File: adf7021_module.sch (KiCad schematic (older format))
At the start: 59 parts, among them J1 Conn_02x10_Counter_Clockwise, J2 Conn_Coaxial, J3 Conn_Coaxial, J4 Conn_02x10_Counter_Clockwise, U1 ADF7021, X1 19.68MHz

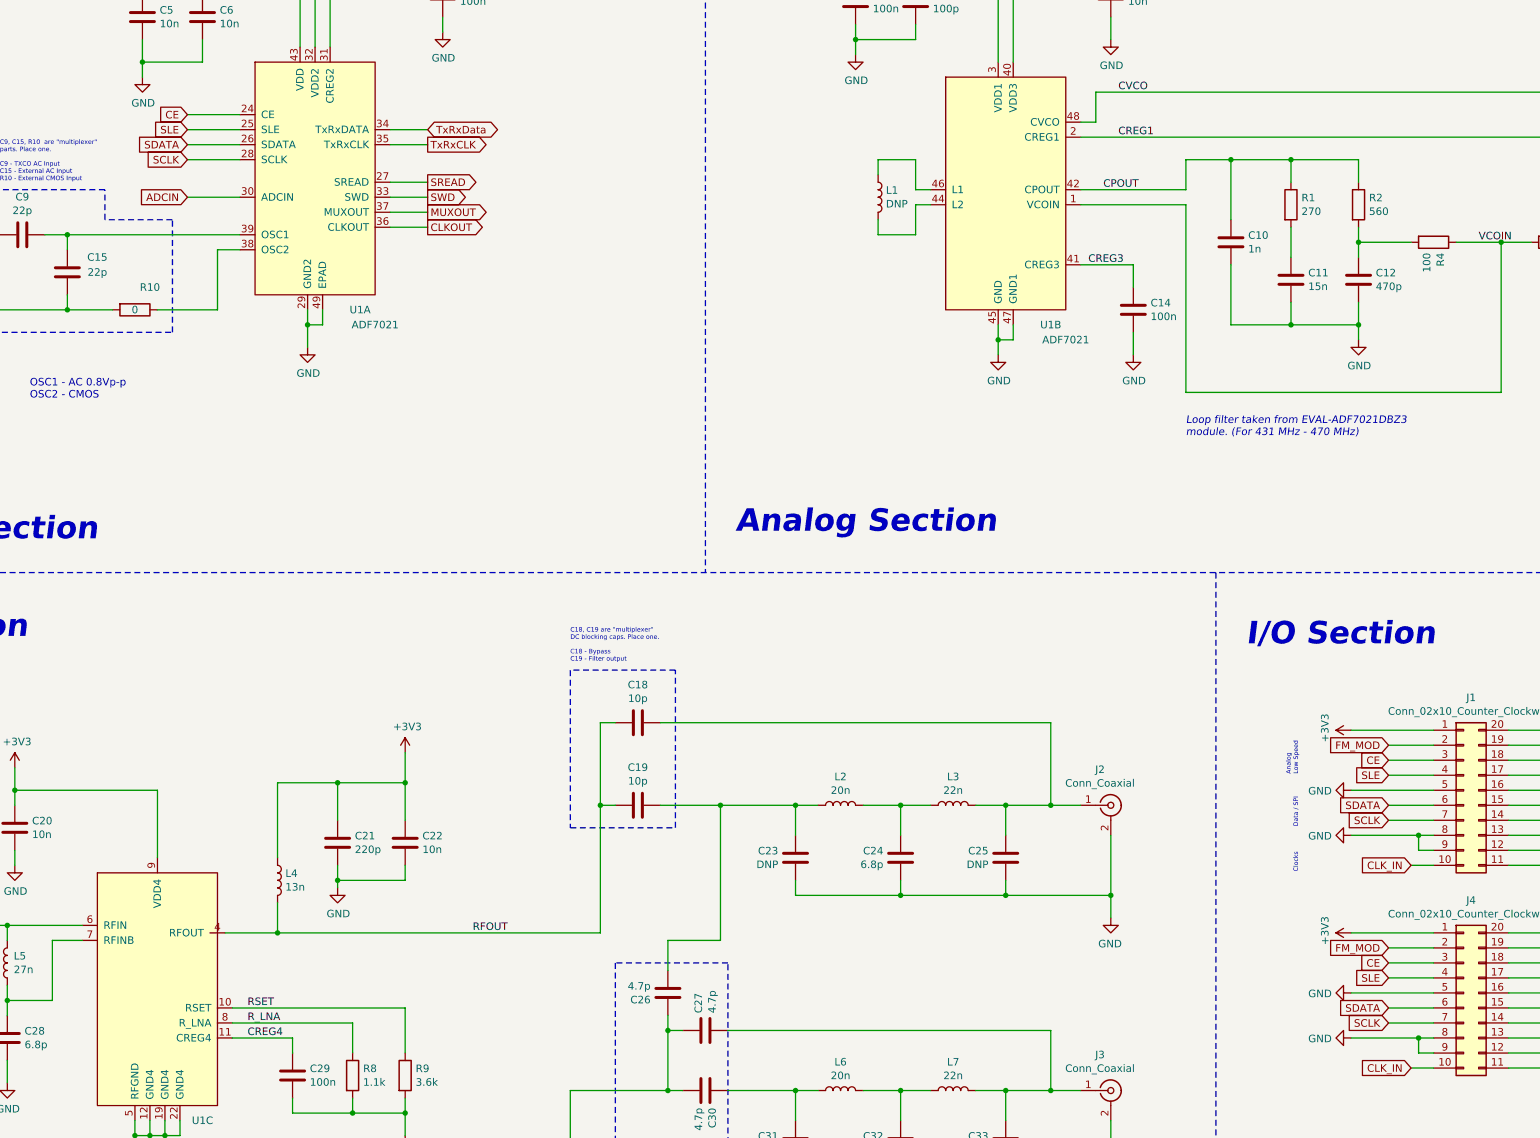
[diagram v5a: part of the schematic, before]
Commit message: Adding series resistors on clock / data pins
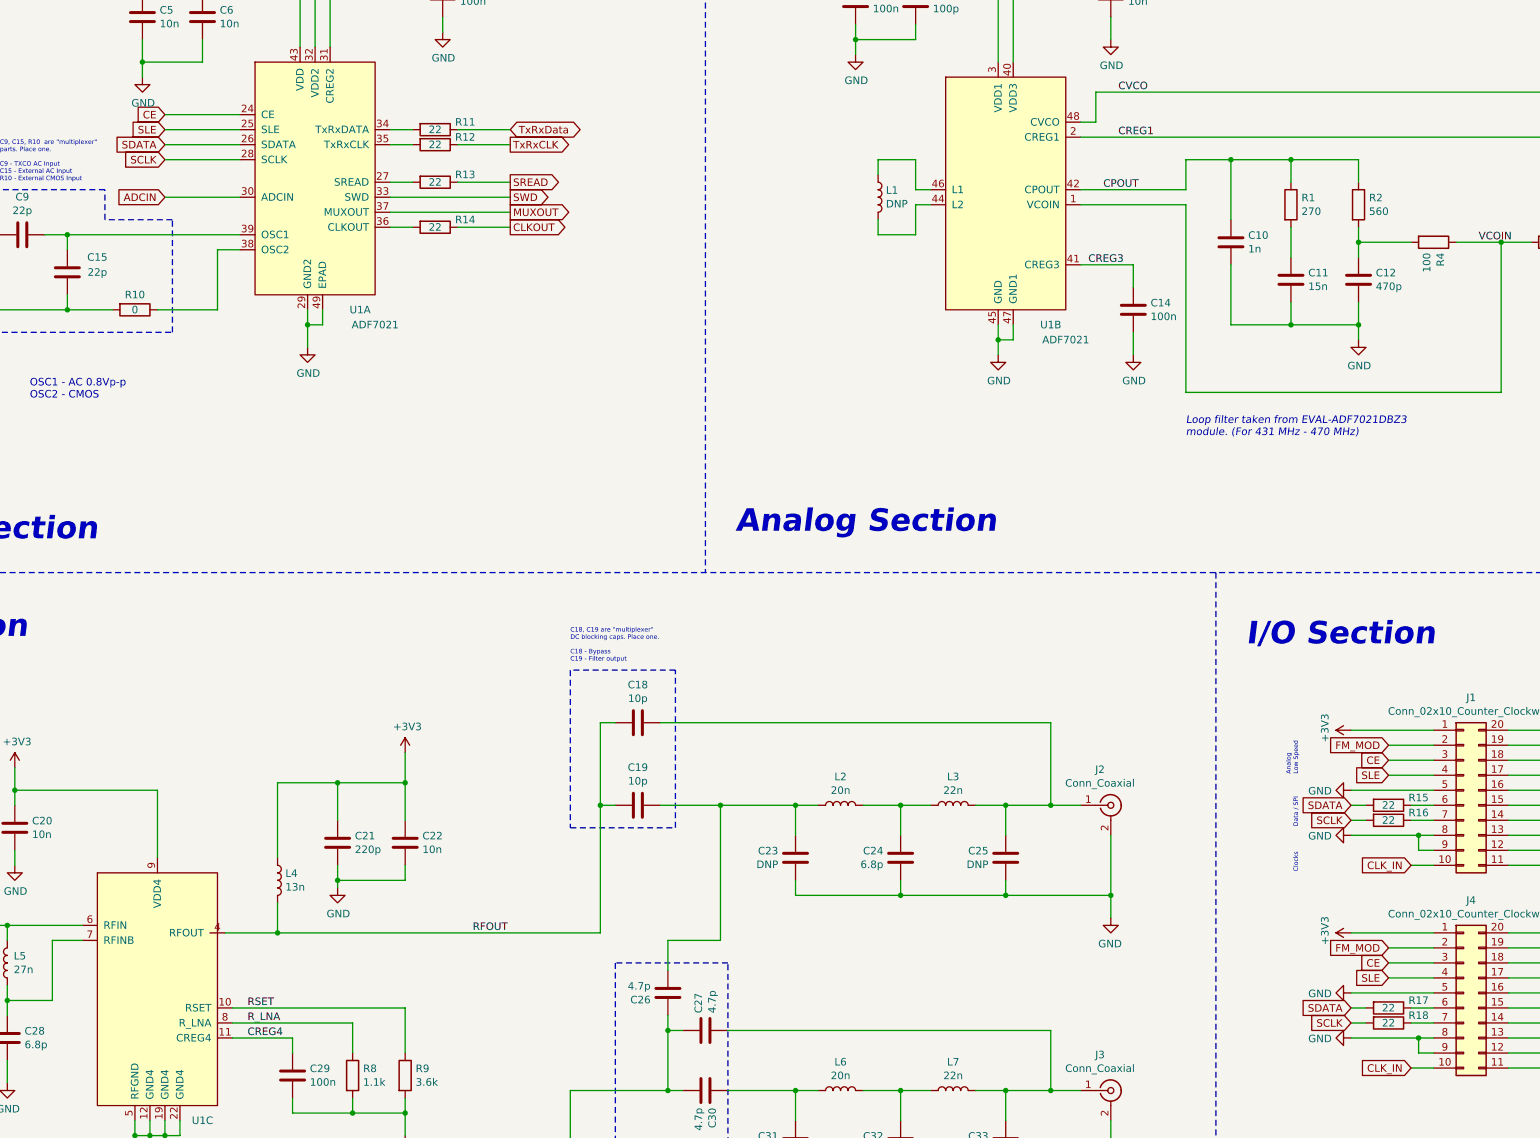
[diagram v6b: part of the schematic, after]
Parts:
- added R11, R12, R13, R14, R15, R16, R17, R18: 22, symbol Device:R
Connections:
- net CLKOUT: now also R14.1; no longer U1.36 (CLKOUT)
- net SCLK: now also R16.2, R18.2; no longer J1.7 (Pin_7), J4.7 (Pin_7)
- net SDATA: now also R15.2, R17.2; no longer J1.6 (Pin_6), J4.6 (Pin_6)
- net SREAD: now also R13.1; no longer U1.27 (SREAD)
- net TxRxCLK: now also R12.1; no longer U1.35 (TxRxCLK)
- net TxRxData: now also R11.1; no longer U1.34 (TxRxDATA)
- new net: R13.2, U1.27 (SREAD)
- new net: R11.2, U1.34 (TxRxDATA)
- new net: R12.2, U1.35 (TxRxCLK)
- new net: R14.2, U1.36 (CLKOUT)
- new net: J1.6 (Pin_6), R15.1
- new net: J1.7 (Pin_7), R16.1
- new net: J4.6 (Pin_6), R17.1
- new net: J4.7 (Pin_7), R18.1
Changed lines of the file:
@@
 Wire Wire Line
 	2450 3750 1800 3750
-Text GLabel 3250 3000 0    50   Input ~ 0
+Text GLabel 3100 3000 0    50   Input ~ 0
 ADCIN
 Wire Wire Line
-	3250 3000 3600 3000
-Text GLabel 3250 2750 0    50   Input ~ 0
+	3100 3000 3600 3000
+Text GLabel 3100 2750 0    50   Input ~ 0
 SCLK
 Wire Wire Line
-	3250 2750 3600 2750
-Text GLabel 3250 2650 0    50   Input ~ 0
+	3100 2750 3600 2750
+Text GLabel 3100 2650 0    50   Input ~ 0
 SDATA
-Text GLabel 3250 2550 0    50   Input ~ 0
+Text GLabel 3100 2550 0    50   Input ~ 0
 SLE
 Wire Wire Line
-	3250 2550 3600 2550
-Wire Wire Line
-	3600 2650 3250 2650
-Text GLabel 3250 2450 0    50   Input ~ 0
+	3100 2550 3600 2550
+Text GLabel 3100 2450 0    50   Input ~ 0
 CE
 Wire Wire Line
-	3250 2450 3600 2450
-Text GLabel 4850 2550 2    50   BiDi ~ 0
+	3100 2450 3600 2450
+Text GLabel 5400 2550 2    50   BiDi ~ 0
 TxRxData
 Wire Wire Line
-	4850 2550 4600 2550
-Text GLabel 4850 2650 2    50   Output ~ 0
+	5400 2550 5050 2550
+Text GLabel 5400 2650 2    50   Output ~ 0
 TxRxCLK
 Wire Wire Line
-	4850 2650 4600 2650
-Text GLabel 4850 2900 2    50   Output ~ 0
+	5400 2650 5050 2650
+Text GLabel 5400 2900 2    50   Output ~ 0
 SREAD
-Text GLabel 4850 3000 2    50   Output ~ 0
+Text GLabel 5400 3000 2    50   Output ~ 0
 SWD
-Text GLabel 4850 3100 2    50   Output ~ 0
+Text GLabel 5400 3100 2    50   Output ~ 0
 MUXOUT
-Text GLabel 4850 3200 2    50   Output ~ 0
+Text GLabel 5400 3200 2    50   Output ~ 0
 CLKOUT
 Wire Wire Line
-	4850 3200 4600 3200
-Wire Wire Line
-	4600 3100 4850 3100
-Wire Wire Line
-	4850 3000 4600 3000
-Wire Wire Line
-	4600 2900 4850 2900
+	5400 3200 5050 3200
+Wire Wire Line
+	4600 3100 5400 3100
+Wire Wire Line
+	5400 3000 4600 3000
+Wire Wire Line
+	4600 2900 4750 2900
 Wire Wire Line
 	3450 3350 3600 3350
@@
 Text GLabel 12350 6650 2    50   Input ~ 0
 ADCIN
-Text GLabel 11250 7150 0    50   Input ~ 0
+Text GLabel 11000 7150 0    50   Input ~ 0
 SCLK
-Text GLabel 11250 7050 0    50   Input ~ 0
+Text GLabel 11000 7050 0    50   Input ~ 0
 SDATA
 Text GLabel 11250 6850 0    50   Input ~ 0
@@
 	12800 6950 12050 6950
 Wire Wire Line
-	11250 7050 11550 7050
-Wire Wire Line
-	11250 7150 11550 7150
+	11000 7050 11100 7050
+Wire Wire Line
+	11000 7150 11100 7150
 $Comp
 L power:GND #PWR028
@@
 U 1 1 603AFF9A
 P 2900 3750
-F 0 "R10" V 2750 3850 50  0000 C CNN
+F 0 "R10" V 2800 3750 50  0000 C CNN
 F 1 "0" V 2900 3750 50  0000 C CNN
 F 2 "" V 2830 3750 50  0001 C CNN
@@
 Text GLabel 12350 8000 2    50   Input ~ 0
 ADCIN
-Text GLabel 11250 8500 0    50   Input ~ 0
+Text GLabel 11000 8500 0    50   Input ~ 0
 SCLK
-Text GLabel 11250 8400 0    50   Input ~ 0
+Text GLabel 11000 8400 0    50   Input ~ 0
 SDATA
 Text GLabel 11250 8200 0    50   Input ~ 0
@@
 	12800 8300 12050 8300
 Wire Wire Line
-	11250 8400 11550 8400
-Wire Wire Line
-	11250 8500 11550 8500
+	11000 8400 11100 8400
+Wire Wire Line
+	11000 8500 11100 8500
 $Comp
 L power:GND #PWR038
@@
 Text Notes 10650 7500 1    30   ~ 0
 Clocks
+$Comp
+L Device:R R14
+U 1 1 60677D63
+P 4900 3200
+F 0 "R14" V 4850 3400 50  0000 C CNN
+F 1 "22" V 4900 3200 50  0000 C CNN
+F 2 "" V 4830 3200 50  0001 C CNN
+F 3 "~" H 4900 3200 50  0001 C CNN
+	1    4900 3200
+	0    1    1    0
+$EndComp
+Wire Wire Line
+	4750 3200 4600 3200
+$Comp
+L Device:R R13
+U 1 1 606926F1
+P 4900 2900
+F 0 "R13" V 4850 3100 50  0000 C CNN
+F 1 "22" V 4900 2900 50  0000 C CNN
+F 2 "" V 4830 2900 50  0001 C CNN
+F 3 "~" H 4900 2900 50  0001 C CNN
+	1    4900 2900
+	0    1    1    0
+$EndComp
+Wire Wire Line
+	5050 2900 5400 2900
+$Comp
+L Device:R R12
+U 1 1 60692CC7
+P 4900 2650
+F 0 "R12" V 4850 2850 50  0000 C CNN
+F 1 "22" V 4900 2650 50  0000 C CNN
+F 2 "" V 4830 2650 50  0001 C CNN
+F 3 "~" H 4900 2650 50  0001 C CNN
+	1    4900 2650
+	0    1    1    0
+$EndComp
+Wire Wire Line
+	4750 2650 4600 2650
+$Comp
+L Device:R R11
+U 1 1 60693127
+P 4900 2550
+F 0 "R11" V 4850 2750 50  0000 C CNN
+F 1 "22" V 4900 2550 50  0000 C CNN
+F 2 "" V 4830 2550 50  0001 C CNN
+F 3 "~" H 4900 2550 50  0001 C CNN
+	1    4900 2550
+	0    1    1    0
+$EndComp
+Wire Wire Line
+	4750 2550 4600 2550
+Wire Wire Line
+	3600 2650 3100 2650
+$Comp
+L Device:R R17
+U 1 1 6070C2A8
+P 11250 8400
+F 0 "R17" V 11200 8600 50  0000 C CNN
+F 1 "22" V 11250 8400 50  0000 C CNN
+F 2 "" V 11180 8400 50  0001 C CNN
+F 3 "~" H 11250 8400 50  0001 C CNN
+	1    11250 8400
+	0    1    1    0
+$EndComp
+Wire Wire Line
+	11400 8400 11550 8400
+$Comp
+L Device:R R18
+U 1 1 60741E3A
+P 11250 8500
+F 0 "R18" V 11200 8700 50  0000 C CNN
+F 1 "22" V 11250 8500 50  0000 C CNN
+F 2 "" V 11180 8500 50  0001 C CNN
+F 3 "~" H 11250 8500 50  0001 C CNN
+	1    11250 8500
+	0    1    1    0
+$EndComp
+Wire Wire Line
+	11400 8500 11550 8500
+$Comp
+L Device:R R15
+U 1 1 607BA8AF
+P 11250 7050
+F 0 "R15" V 11200 7250 50  0000 C CNN
+F 1 "22" V 11250 7050 50  0000 C CNN
+F 2 "" V 11180 7050 50  0001 C CNN
+F 3 "~" H 11250 7050 50  0001 C CNN
+	1    11250 7050
+	0    1    1    0
+$EndComp
+Wire Wire Line
+	11400 7050 11550 7050
+$Comp
+L Device:R R16
+U 1 1 607BB020
+P 11250 7150
+F 0 "R16" V 11200 7350 50  0000 C CNN
+F 1 "22" V 11250 7150 50  0000 C CNN
+F 2 "" V 11180 7150 50  0001 C CNN
+F 3 "~" H 11250 7150 50  0001 C CNN
+	1    11250 7150
+	0    1    1    0
+$EndComp
+Wire Wire Line
+	11400 7150 11550 7150
 $EndSCHEMATC
